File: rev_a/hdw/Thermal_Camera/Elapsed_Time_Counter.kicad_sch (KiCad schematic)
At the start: 7 parts

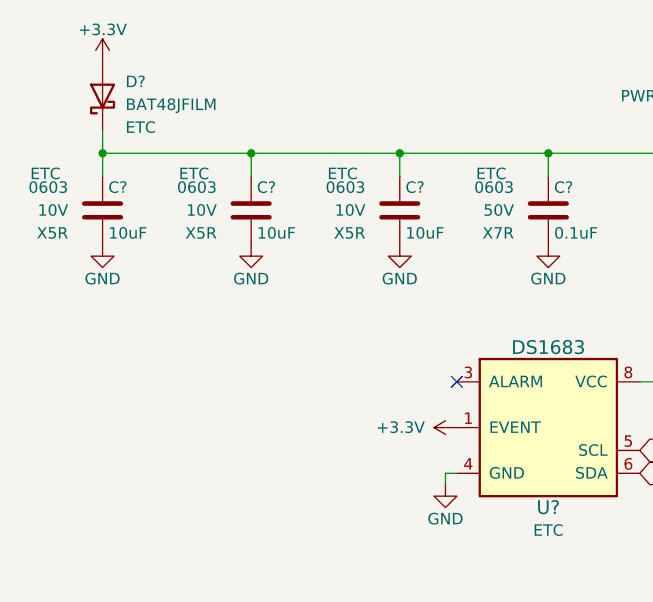
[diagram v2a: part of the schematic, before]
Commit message: changed a lot of circuits from +3.3V to +3.0V VDD
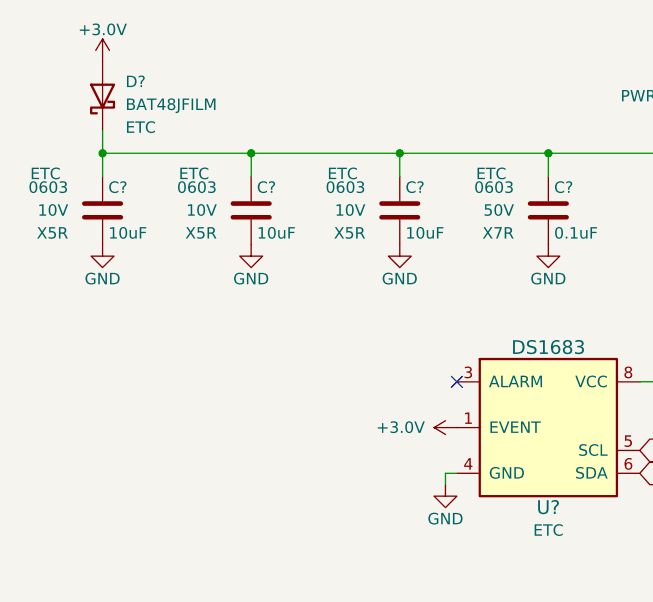
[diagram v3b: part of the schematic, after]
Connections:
- net +3.3V renamed +3.0V
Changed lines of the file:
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@@
+    )
+  )
+  (symbol (lib_id "Custom Library:+3.0V") (at 95.25 59.69 0) (unit 1)
+    (in_bom yes) (on_board yes) (dnp no)
+    (property "Reference" "#PWR02301" (at 95.25 63.5 0)
+      (effects (font (size 1.27 1.27)) hide)
+    )
+    (property "Value" "+3.0V" (at 95.25 56.134 0)
+      (effects (font (size 1.27 1.27)))
+    )
+    (property "Footprint" "" (at 95.25 59.69 0)
+      (effects (font (size 1.27 1.27)) hide)
+    )
+    (property "Datasheet" "" (at 95.25 59.69 0)
+      (effects (font (size 1.27 1.27)) hide)
+    )
+    (pin "1")
+    (instances
+      (project "Thermal_Camera"
+        (path "/4bd21e0b-5408-4b93-866e-c82ac5b31fa9/e683c214-7fe6-4d85-9668-46cd89bb0f39"
+          (reference "#PWR02301") (unit 1)
+        )
+      )
     )
   )
@@
     )
   )
-  (symbol (lib_id "power:+3.3V") (at 134.62 100.33 90) (unit 1)
-    (in_bom yes) (on_board yes) (dnp no)
-    (property "Reference" "#PWR?" (at 138.43 100.33 0)
-      (effects (font (size 1.27 1.27)) hide)
-    )
-    (property "Value" "+3.3V" (at 131.064 100.33 90)
+  (symbol (lib_id "Custom Library:+3.0V") (at 134.62 100.33 90) (unit 1)
+    (in_bom yes) (on_board yes) (dnp no)
+    (property "Reference" "#PWR02302" (at 138.43 100.33 0)
+      (effects (font (size 1.27 1.27)) hide)
+    )
+    (property "Value" "+3.0V" (at 131.064 100.33 90)
       (effects (font (size 1.27 1.27)) (justify left))
     )
@@
     (pin "1")
     (instances
-      (project "VFD_Clock"
-        (path "/0e0fa043-3ab8-4cb9-8105-f968ef03a597/00000000-0000-0000-0000-00005e07b870"
-          (reference "#PWR?") (unit 1)
-        )
-      )
-      (project "Nixie_Clock_Core"
-        (path "/16fdce21-b570-4d81-a458-e8839d611806/61f04371-5be4-452b-bab3-2ded046cc354"
-          (reference "#PWR01406") (unit 1)
-        )
-      )
-      (project "Thermal_Camera"
-        (path "/4bd21e0b-5408-4b93-866e-c82ac5b31fa9/e683c214-7fe6-4d85-9668-46cd89bb0f39"
-          (reference "#PWR01706") (unit 1)
+      (project "Thermal_Camera"
+        (path "/4bd21e0b-5408-4b93-866e-c82ac5b31fa9/e683c214-7fe6-4d85-9668-46cd89bb0f39"
+          (reference "#PWR02302") (unit 1)
         )
       )
@@
         )
       )
-    )
-  )
-  (symbol (lib_id "power:+3.3V") (at 95.25 59.69 0) (unit 1)
-    (in_bom yes) (on_board yes) (dnp no)
-    (property "Reference" "#PWR?" (at 95.25 63.5 0)
-      (effects (font (size 1.27 1.27)) hide)
-    )
-    (property "Value" "+3.3V" (at 95.25 56.134 0)
-      (effects (font (size 1.27 1.27)))
-    )
-    (property "Footprint" "" (at 95.25 59.69 0)
-      (effects (font (size 1.27 1.27)) hide)
-    )
-    (property "Datasheet" "" (at 95.25 59.69 0)
-      (effects (font (size 1.27 1.27)) hide)
-    )
-    (pin "1")
-    (instances
-      (project "VFD_Clock"
-        (path "/0e0fa043-3ab8-4cb9-8105-f968ef03a597/00000000-0000-0000-0000-00005e07b870"
-          (reference "#PWR?") (unit 1)
-        )
-      )
-      (project "Nixie_Clock_Core"
-        (path "/16fdce21-b570-4d81-a458-e8839d611806/61f04371-5be4-452b-bab3-2ded046cc354"
-          (reference "#PWR01401") (unit 1)
-        )
-      )
-      (project "Thermal_Camera"
-        (path "/4bd21e0b-5408-4b93-866e-c82ac5b31fa9/e683c214-7fe6-4d85-9668-46cd89bb0f39"
-          (reference "#PWR01701") (unit 1)
-        )
-      )

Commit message: added some more USB stuff
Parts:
- added C503: 0.1uF, Capacitors_SMD:C_0603, symbol Custom_Library:C_Custom
- added DOC502: TBD, symbol Custom_Library:I2C_Address
- added U502: MCP9804, Package_DFN_QFN:DFN-8-1EP_3x2mm_P0.5mm_EP1.3x1.5mm, symbol Sensor_Temperature:MCP9804_DFN
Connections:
- net +3.0V: now also C503.1, U502.8 (V_{DD})
- net GND: now also C503.2, U502.4 (GND), U502.9 (EP/GND)
- net I2C_SCL: now also U502.2 (SCL)
- net I2C_SDA: now also U502.1 (SDA)
- no-connect marks 1 -> 2
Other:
- note added: "Ambient, place away from power components"
- moved on the sheet: C?, D?, U?

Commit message: lots of random schematic progress
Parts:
- added J?: VOSPI, symbol Connector_Generic:Conn_01x04
- added J?: FLASH SPI, symbol Connector_Generic:Conn_01x04
- added J?: I2C, symbol Connector_Generic:Conn_01x03
- added J?: UART, symbol Connector_Generic:Conn_01x03
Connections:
- net GND: now also J?.3 (Pin_3), J?.3 (Pin_3), J?.4 (Pin_4), J?.4 (Pin_4)
- net I2C_SCL: now also J?.2 (Pin_2)
- net I2C_SDA: now also J?.1 (Pin_1)
- new net FLASH_SPI_MISO: J?.2 (Pin_2)
- new net FLASH_SPI_MOSI: J?.1 (Pin_1)
- new net FLASH_SPI_SCK: J?.3 (Pin_3)
- new net FLIR_VOSPI_CLK: J?.3 (Pin_3)
- new net FLIR_VOSPI_MISO: J?.2 (Pin_2)
- new net FLIR_VOSPI_MOSI: J?.1 (Pin_1)
- new net USB_UART_RX: J?.1 (Pin_1)
- new net USB_UART_TX: J?.2 (Pin_2)
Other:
- moved on the sheet: C503, C?, D?, U502, U?

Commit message: lots of schematic progress
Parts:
- C? (x3): footprint Capacitors_SMD:C_0603 -> (none); Digi-Key PN 1276-1871-1-ND -> (none); display_footprint 0603 -> (none)
- C?: footprint Capacitors_SMD:C_0603 -> (none); Digi-Key PN 1276-1935-1-ND -> (none); display_footprint 0603 -> (none)
- C?: renamed from C503; footprint Capacitors_SMD:C_0603 -> (none); Digi-Key PN 1276-1935-1-ND -> (none); display_footprint 0603 -> (none)
- DOC?: renamed from DOC502; value TBD -> 0x1F
- gave numbers to parts that had none: 4
- renumbered U502 to U?
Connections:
- net +3.0V: now also U?.5 (A2), U?.6 (A1), U?.7 (A0)
